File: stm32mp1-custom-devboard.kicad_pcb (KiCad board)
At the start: 4 copper layers, 120 x 80.6 mm, 137 parts, among them Con1 52746-0671, Con2 505110-2491, Con3 2041119-1, Con4 USB_C_Wurth_632723130112, Con5 USB_C_Wurth_632723130112, P1 Main Power Supply, Q1 BC847B, T2 WE-RJ45_74990101210, U1 TPS61169DCKR, U2 MCP1703T-3302E, U3 ST1S10PHR, U4 ST1S09IPUR, U5 STM32F103C(8-B)Tx, U6 MCP1700T-3302E_MB, U7 KSZ8041NL_RNL, U8 USBLC6-2, U9 USBLC6-2, X1 8.000MHZ, X2 ECS-2016MV-250-CN-TR

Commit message: Schematic finished, elements figurated on pcb, tracking started
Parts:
- added C54: 100n, Capacitors_Smd_0603:100nF_0603, F.Cu at (135.6, 135.4)
- added C55: 100n, Capacitors_Smd_0603:100nF_0603, F.Cu at (118.2, 133.8)
- added C56: 100n, Capacitors_Smd_0603:100nF_0603, F.Cu at (116.6, 133.2)
- added R51: 10k, Resistor_Smd_0603:10k_0603, F.Cu at (131.3, 128.7)
- added R52: 10k, Resistor_Smd_0603:10k_0603, F.Cu at (131.3, 126.2)
- added R53: 10k, Resistor_Smd_0603:10k_0603, F.Cu at (131.3, 133.7)
- added R54: 10k, Resistor_Smd_0603:10k_0603, F.Cu at (131.3, 131.2)
- added R55: 10k, Resistor_Smd_0603:10k_0603, F.Cu at (115.0, 131.0)
- added R56: 10k, Resistor_Smd_0603:10k_0603, F.Cu at (117.8, 130.2)
- added U10: APX803D-29SRG-7, Reset_Device_Diodes:APX803D-29SRG-7, F.Cu at (133.1, 136.0)
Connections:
- Con1 pad 6: /STM32MP1 module/PF10_GPIO -> /STM32MP1 module/PA9-GPIO
- Con2 pad 12: /LCD+Touchscreen/LCD_RESET -> /RESET
- Con3 pad 1: (no net) -> /STM32MP1 module/PE3-GPIO
- Con3 pad 10: (no net) -> /STM32MP1 module/SPI1_NSS
- Con3 pad 11: (no net) -> /STM32MP1 module/UART8-TXD
- Con3 pad 12: (no net) -> /STM32MP1 module/SPI1_MOSI
- Con3 pad 13: (no net) -> /STM32MP1 module/UART8-RXD
- Con3 pad 14: (no net) -> /STM32MP1 module/SPI1_MISO
- Con3 pad 15: (no net) -> GND
- Con3 pad 16: (no net) -> /STM32MP1 module/SPI1_SCK
- Con3 pad 18: (no net) -> GND
- Con3 pad 2: (no net) -> 3V3
- Con3 pad 20: (no net) -> /STM32MP1 module/PC7-GPIO
- Con3 pad 21: (no net) -> GND
- Con3 pad 22: (no net) -> /RESET
- Con3 pad 23: (no net) -> /STM32MP1 module/UART8-RTS
- Con3 pad 24: (no net) -> 3V3
- Con3 pad 25: (no net) -> /STM32MP1 module/UART8-CTS
- Con3 pad 26: (no net) -> GND
- Con3 pad 27: (no net) -> GND
- Con3 pad 29: (no net) -> GND
- Con3 pad 30: (no net) -> /MiniPci Module/I2C-SCL
- Con3 pad 32: (no net) -> /MiniPci Module/I2C-SDA
- Con3 pad 34: (no net) -> GND
- Con3 pad 35: (no net) -> GND
- Con3 pad 36: (no net) -> /USB Module/USB-A-D_M
- Con3 pad 37: (no net) -> GND
- Con3 pad 38: (no net) -> /USB Module/USB-A-D_P
- Con3 pad 39: (no net) -> 3V3
- Con3 pad 4: (no net) -> GND
- Con3 pad 40: (no net) -> GND
- Con3 pad 41: (no net) -> 3V3
- Con3 pad 42: (no net) -> /MiniPci Module/NETLIGHT
- Con3 pad 43: (no net) -> GND
- Con3 pad 45: (no net) -> /STM32MP1 module/PE14-GPIO
- Con3 pad 50: (no net) -> GND
- Con3 pad 52: (no net) -> 3V3
- Con3 pad 8: (no net) -> /PE15
- Con3 pad 9: (no net) -> GND
- Con5 pad A5: /USB Module/USB-C-ID -> /STM32MP1 module/PA0-GPIO
- Con5 pad B5: /USB Module/USB-C-ID -> /STM32MP1 module/PA0-GPIO
- R23 pad 1: /STLink Module/JTMS -> /STM32MP1 module/JTAG-TMS
- R34 pad 2: /Ethernet Module/ENET_MDC -> /STM32MP1 module/ENET1-MDC
- R50 pad 2: /USB Module/USB-C-ID -> /STM32MP1 module/PA0-GPIO
- SOM1 pad 10: (no net) -> Net-(R55-Pad2)
- SOM1 pad 100: Net-(SOM1-Pad100) -> 5V
- SOM1 pad 101: (no net) -> /Ethernet Module/ENET-CRS-DV
- SOM1 pad 102: Net-(SOM1-Pad100) -> 5V
- SOM1 pad 104: Net-(SOM1-Pad100) -> 5V
- SOM1 pad 106: Net-(SOM1-Pad100) -> 5V
- SOM1 pad 108: Net-(SOM1-Pad100) -> 5V
- SOM1 pad 109: (no net) -> /Arduino Shield Module/GPIO-D5
- SOM1 pad 110: Net-(SOM1-Pad100) -> 5V
- SOM1 pad 112: Net-(SOM1-Pad100) -> 5V
- SOM1 pad 113: (no net) -> /Arduino Shield Module/ATN
- SOM1 pad 114: (no net) -> /Ethernet Module/ENET-TXEN
- SOM1 pad 118: (no net) -> /STM32MP1 module/SPI1_MOSI
- SOM1 pad 119: (no net) -> /Ethernet Module/ENET-TXD2
- SOM1 pad 122: (no net) -> /Arduino Shield Module/GPIO-D6
- SOM1 pad 124: (no net) -> /Ethernet Module/ENET-TXD1
- SOM1 pad 129: (no net) -> /STM32MP1 module/PA9-GPIO
- SOM1 pad 131: (no net) -> /Arduino Shield Module/GPIO-D13
- SOM1 pad 134: (no net) -> /PE15
- SOM1 pad 137: (no net) -> /Arduino Shield Module/SPI-SCK
- SOM1 pad 138: (no net) -> /Ethernet Module/ENET-RXD2
- SOM1 pad 139: (no net) -> /STM32MP1 module/ADC1_INP2
- SOM1 pad 140: (no net) -> /STM32MP1 module/ADC1_INP19
- SOM1 pad 141: (no net) -> /STM32MP1 module/PC7-GPIO
- SOM1 pad 148: (no net) -> /Arduino Shield Module/GPIO-D11
- SOM1 pad 149: (no net) -> /STM32MP1 module/ADC1_INP15
- SOM1 pad 150: (no net) -> /Ethernet Module/ENET-RXER
- SOM1 pad 151: (no net) -> /Ethernet Module/ENET-TXD3
- SOM1 pad 152: (no net) -> /STM32MP1 module/ADC1_INP3
- SOM1 pad 154: (no net) -> /Arduino Shield Module/SPI-MISO
- SOM1 pad 157: /LCD+Touchscreen/LCD_RESET -> /Ethernet Module/ENET-REFCLK
- SOM1 pad 158: (no net) -> /Ethernet Module/ENET-IRQ
- SOM1 pad 160: (no net) -> /Arduino Shield Module/GPIO-D12
- SOM1 pad 161: (no net) -> /STM32MP1 module/PE14-GPIO
- SOM1 pad 162: (no net) -> /STM32MP1 module/SPI1_NSS
- SOM1 pad 163: (no net) -> /MiniPci Module/NETLIGHT
- SOM1 pad 164: (no net) -> /Arduino Shield Module/SPI-MOSI
- SOM1 pad 166: (no net) -> /Arduino Shield Module/I2C-SDA
- SOM1 pad 167: (no net) -> /Arduino Shield Module/UART-RX0
- SOM1 pad 169: (no net) -> /STM32MP1 module/SPI1_MISO
- SOM1 pad 171: (no net) -> /Arduino Shield Module/UART-TX0
- SOM1 pad 173: (no net) -> /Arduino Shield Module/GPIO-D3
- SOM1 pad 175: (no net) -> /STM32MP1 module/SPI1_SCK
- SOM1 pad 179: (no net) -> /STM32MP1 module/PE3-GPIO
- SOM1 pad 19: (no net) -> /USB Module/USB-C-D_P
- SOM1 pad 21: (no net) -> /USB Module/USB-C-D_M
- SOM1 pad 25: (no net) -> /USB Module/USB-A-D_P
- SOM1 pad 27: (no net) -> /USB Module/USB-A-D_M
- SOM1 pad 4: (no net) -> /RESET
- SOM1 pad 45: (no net) -> /Arduino Shield Module/GPIO-D4
- SOM1 pad 46: (no net) -> /STM32MP1 module/JTAG-TMS
- SOM1 pad 47: (no net) -> /STM32MP1 module/ADC1_INP13
- SOM1 pad 48: (no net) -> /STM32MP1 module/JTAG-~TRST~
- SOM1 pad 52: (no net) -> /STM32MP1 module/JTAG-TDO
- SOM1 pad 53: (no net) -> /STM32MP1 module/ENET1-MDC
- SOM1 pad 54: (no net) -> /STM32MP1 module/JTAG-TCK
- SOM1 pad 55: (no net) -> /STM32MP1 module/ADC2_INP10
- SOM1 pad 57: (no net) -> /STM32MP1 module/UART8-TXD
- SOM1 pad 58: (no net) -> /Ethernet Module/ENET-RXD3
- SOM1 pad 6: (no net) -> Net-(C55-Pad1)
- SOM1 pad 61: (no net) -> /Ethernet Module/ENET-MDIO
- SOM1 pad 62: (no net) -> /STM32MP1 module/PA0-GPIO
- SOM1 pad 63: (no net) -> /STM32MP1 module/UART8-RXD
- SOM1 pad 64: /STM32MP1 module/PF10_GPIO -> /Arduino Shield Module/GPIO-D2
- SOM1 pad 65: (no net) -> /Arduino Shield Module/GPIO-D8
- SOM1 pad 66: (no net) -> /STM32MP1 module/UART8-CTS
- SOM1 pad 67: (no net) -> /Arduino Shield Module/GPIO-D7
- SOM1 pad 69: (no net) -> /Arduino Shield Module/SPI-RST
- SOM1 pad 7: (no net) -> Net-(R53-Pad2)
- SOM1 pad 72: (no net) -> /Arduino Shield Module/GPIO-D10
- SOM1 pad 73: (no net) -> /Arduino Shield Module/I2C-SCL
- SOM1 pad 74: (no net) -> /STM32MP1 module/UART8-RTS
- SOM1 pad 75: (no net) -> /STLink Module/STLINK_RX
- SOM1 pad 76: (no net) -> /MiniPci Module/I2C-SCL
- SOM1 pad 77: (no net) -> /STLink Module/STLINK_TX
- SOM1 pad 78: (no net) -> /Arduino Shield Module/GPIO-D9
- SOM1 pad 79: (no net) -> /Ethernet Module/ENET-TXD0
- SOM1 pad 8: (no net) -> Net-(C56-Pad1)
- SOM1 pad 80: (no net) -> /MiniPci Module/I2C-SDA
- SOM1 pad 9: (no net) -> Net-(R51-Pad2)
- SOM1 pad 96: Net-(SOM1-Pad100) -> 5V
- SOM1 pad 97: (no net) -> /Ethernet Module/ENET-RXD0
- SOM1 pad 98: Net-(SOM1-Pad100) -> 5V
- SOM1 pad 99: (no net) -> /Ethernet Module/ENET-RXD1
- U5 pad 12: (no net) -> /STLink Module/STLINK_TX
- U5 pad 13: (no net) -> /STLink Module/STLINK_RX
- U5 pad 18: (no net) -> /STM32MP1 module/JTAG-~TRST~
- U5 pad 26: (no net) -> /STM32MP1 module/JTAG-TCK
- U5 pad 27: /STLink Module/JTMS -> /STM32MP1 module/JTAG-TMS
- U5 pad 31: (no net) -> /STM32MP1 module/JTAG-TDO
- U7 pad 12: /Ethernet Module/ENET_MDC -> /STM32MP1 module/ENET1-MDC
- U7 pad 23: (no net) -> /Ethernet Module/ENET-TXEN
- U7 pad 24: (no net) -> /Ethernet Module/ENET-TXD0
- U7 pad 25: (no net) -> /Ethernet Module/ENET-TXD1
- U7 pad 26: (no net) -> /Ethernet Module/ENET-TXD2
- U7 pad 27: (no net) -> /Ethernet Module/ENET-TXD3
- U8 pad 1: (no net) -> /USB Module/USB-C-D_M
- U8 pad 3: (no net) -> /USB Module/USB-C-D_P
- U9 pad 1: (no net) -> /USB Module/USB-A-D_M
- U9 pad 3: (no net) -> /USB Module/USB-A-D_P
- XA1 pad A0: (no net) -> /STM32MP1 module/ADC1_INP2
- XA1 pad A1: (no net) -> /STM32MP1 module/ADC2_INP10
- XA1 pad A2: (no net) -> /STM32MP1 module/ADC1_INP13
- XA1 pad A3: (no net) -> /STM32MP1 module/ADC1_INP15
- XA1 pad A4: (no net) -> /STM32MP1 module/ADC1_INP3
- XA1 pad A5: (no net) -> /STM32MP1 module/ADC1_INP19
- XA1 pad ATN: (no net) -> /Arduino Shield Module/ATN
- XA1 pad D0: (no net) -> /Arduino Shield Module/UART-RX0
- XA1 pad D1: (no net) -> /Arduino Shield Module/UART-TX0
- XA1 pad D10: (no net) -> /Arduino Shield Module/GPIO-D10
- XA1 pad D11: (no net) -> /Arduino Shield Module/GPIO-D11
- XA1 pad D12: (no net) -> /Arduino Shield Module/GPIO-D12
- XA1 pad D13: (no net) -> /Arduino Shield Module/GPIO-D13
- XA1 pad D2: (no net) -> /Arduino Shield Module/GPIO-D2
- XA1 pad D3: (no net) -> /Arduino Shield Module/GPIO-D3
- XA1 pad D4: (no net) -> /Arduino Shield Module/GPIO-D4
- XA1 pad D5: (no net) -> /Arduino Shield Module/GPIO-D5
- XA1 pad D6: (no net) -> /Arduino Shield Module/GPIO-D6
- XA1 pad D7: (no net) -> /Arduino Shield Module/GPIO-D7
- XA1 pad D8: (no net) -> /Arduino Shield Module/GPIO-D8
- XA1 pad D9: (no net) -> /Arduino Shield Module/GPIO-D9
- XA1 pad IORF: (no net) -> /PE15
- XA1 pad MISO: (no net) -> /Arduino Shield Module/SPI-MISO
- XA1 pad MOSI: (no net) -> /Arduino Shield Module/SPI-MOSI
- XA1 pad RST1: (no net) -> /RESET
- XA1 pad RST2: (no net) -> /Arduino Shield Module/SPI-RST
- XA1 pad SCK: (no net) -> /Arduino Shield Module/SPI-SCK
- XA1 pad SCL: (no net) -> /Arduino Shield Module/I2C-SCL
- XA1 pad SDA: (no net) -> /Arduino Shield Module/I2C-SDA

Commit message: Tracking in progress
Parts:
- moved C54 2.88 mm to (136.2, 132.6), turned to 180 degrees
- moved R8 1.52 mm to (185.5, 108.5)
- moved R7 1.33 mm to (186.9, 108.5)
- moved C9 0.26 mm to (139.2, 98.9)
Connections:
- Con5 pad B3: (no net) -> /STM32MP1 module/PA0-GPIO
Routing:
- net GND: track 0.00 -> 157.2 mm, vias 0 -> 77
- net 3V3: track 0.00 -> 131.5 mm, vias 0 -> 10
- net /LCD+Touchscreen/Touchscreen Power Supply/VOUT_3.3V_250mA: track 0.00 -> 47.7 mm
- net 5V: track 0.00 -> 44.7 mm, vias 0 -> 11
- net VPP: track 0.00 -> 35.5 mm, vias 0 -> 3
- net /LCD+Touchscreen/LCD Backlight Controller/BACKLIGHT_HIGH: track 0.00 -> 28.9 mm, vias 0 -> 2
- net /LCD+Touchscreen/LCD Backlight Controller/BACKLIGHT_LOW: track 0.00 -> 28.7 mm, vias 0 -> 2
- net Net-(C10-Pad1): track 0.00 -> 28.0 mm, vias 0 -> 2
- net Net-(C49-Pad2): track 0.00 -> 25.7 mm
- net Net-(C26-Pad2): track 0.00 -> 25.7 mm
- net Net-(C6-Pad1): track 0.00 -> 18.7 mm
- net /STM32MP1 module/PA0-GPIO: track 0.00 -> 18.2 mm, vias 0 -> 3
- net Net-(C45-Pad2): track 0.00 -> 17.0 mm
- net /RESET: track 0.00 -> 15.0 mm
- net Net-(C15-Pad2): track 0.00 -> 14.9 mm, vias 0 -> 2
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- added copper zone on In1.Cu, net 5V
- removed copper zone on In1.Cu, net 3V3
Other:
- net class USB-C added: clearance 0.152, trace_width 0.152, via_dia 0.45, via_drill 0.2
- rule trace_min: 0.2 -> 0.152

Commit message: Tracking in progress
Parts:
- moved R94 2.54 mm to (194.3, 130.4), turned to 0 degrees
- moved R49 2.52 mm to (193.5, 127.8), turned to 90 degrees
- moved R48 1.56 mm to (194.3, 129.4), turned to 0 degrees
- moved R96 1.44 mm to (194.5, 127.8), turned to 90 degrees
- moved R27 0.39 mm to (185.6, 132.2)
- moved C35 0.37 mm to (193.9, 131.6)
- moved R41 0.24 mm to (191.8, 126.2)
- moved C12 0.12 mm to (146.5, 108.6)
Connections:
- net /USB Module/USB-A-D_M renamed /USB Module/USB-A-D_N
- net /USB Module/USB-C-D_M renamed /USB Module/USB-C-D_N
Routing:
- net 3V3: track 131.5 -> 442.6 mm, vias 10 -> 28
- net /Arduino Shield Module/UART-RX0: track 0.00 -> 132.7 mm, vias 0 -> 3
- net /Arduino Shield Module/UART-TX0: track 0.00 -> 129.7 mm, vias 0 -> 3
- net /Arduino Shield Module/GPIO-D3: track 0.00 -> 127.5 mm, vias 0 -> 3
- net /Arduino Shield Module/SPI-MISO: track 0.00 -> 102.9 mm, vias 0 -> 1
- net /Arduino Shield Module/SPI-MOSI: track 0.00 -> 102.9 mm, vias 0 -> 1
- net /LCD+Touchscreen/LCD_MIPI_D0-: track 0.00 -> 97.2 mm, vias 0 -> 2
- net /LCD+Touchscreen/LCD_MIPI_D0+: track 0.00 -> 93.3 mm, vias 0 -> 2
- net /LCD+Touchscreen/LCD_MIPI_D1-: track 0.00 -> 89.9 mm, vias 0 -> 2
- net /Arduino Shield Module/GPIO-D6: track 0.00 -> 89.3 mm, vias 0 -> 3
- net /USB Module/USB-C-D_P: track 0.00 -> 87.7 mm, vias 0 -> 2
- net /Arduino Shield Module/SPI-SCK: track 0.00 -> 87.6 mm, vias 0 -> 4
- net /LCD+Touchscreen/LCD_MIPI_D1+: track 0.00 -> 86.7 mm, vias 0 -> 2
- net /USB Module/USB-C-D_N: track 0.00 -> 85.6 mm, vias 0 -> 2
- net /Arduino Shield Module/GPIO-D2: track 0.00 -> 80.2 mm, vias 0 -> 1
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
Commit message: Tracking almost finished
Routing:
- net /Ethernet Module/ENET-TXD1: track 0.98 -> 130.9 mm, vias 1 -> 4
- net /Ethernet Module/ENET-TXD3: track 3.03 -> 132.4 mm, vias 1 -> 8
- net /STM32MP1 module/JTAG-TMS: track 2.84 -> 131.2 mm, vias 0 -> 4
- net /Ethernet Module/ENET-IRQ: track 2.15 -> 126.5 mm, vias 0 -> 4
- net /STM32MP1 module/JTAG-TDO: track 0.00 -> 124.2 mm, vias 0 -> 4
- net /Ethernet Module/ENET-TXD0: track 0.66 -> 119.1 mm, vias 1 -> 4
- net /LCD+Touchscreen/LCD_BACKLIGHT_PWM: track 0.00 -> 116.0 mm, vias 0 -> 4
- net /STM32MP1 module/JTAG-TCK: track 0.00 -> 111.7 mm, vias 0 -> 4
- net /Ethernet Module/ENET-RXER: track 8.61 -> 119.4 mm, vias 0 -> 4
- net /STM32MP1 module/JTAG-~TRST~: track 0.00 -> 109.2 mm, vias 0 -> 4
- net /Ethernet Module/ENET-TXEN: track 0.75 -> 108.6 mm, vias 1 -> 4
- net /STM32MP1 module/PA0-GPIO: track 18.2 -> 122.2 mm, vias 3 -> 6
- net /STM32MP1 module/PE2_I2C4_SDA: track 12.0 -> 114.9 mm, vias 0 -> 8
- net /Ethernet Module/ENET-RXD2: track 6.93 -> 108.5 mm, vias 2 -> 7
- net /STM32MP1 module/PA9-GPIO: track 0.69 -> 100.0 mm, vias 1 -> 6
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
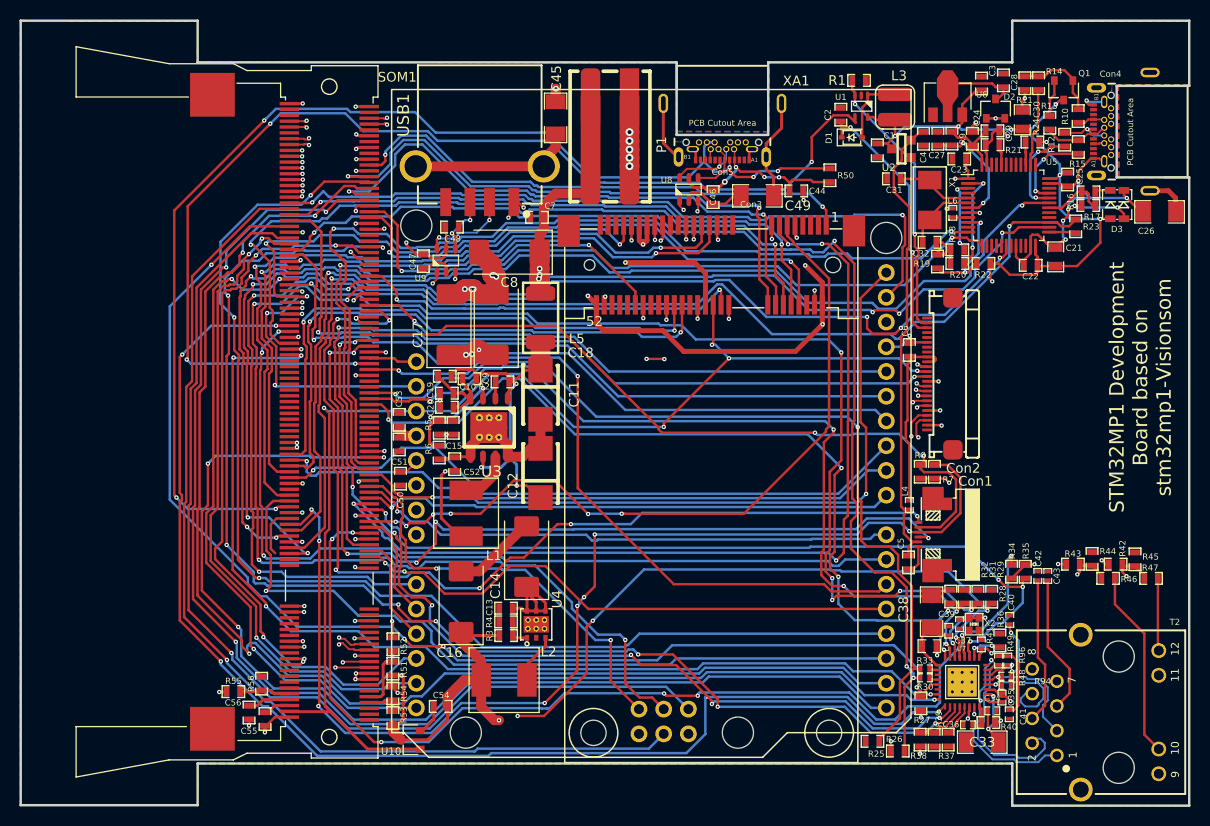
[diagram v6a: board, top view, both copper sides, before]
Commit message: Tracking finished, started tunning
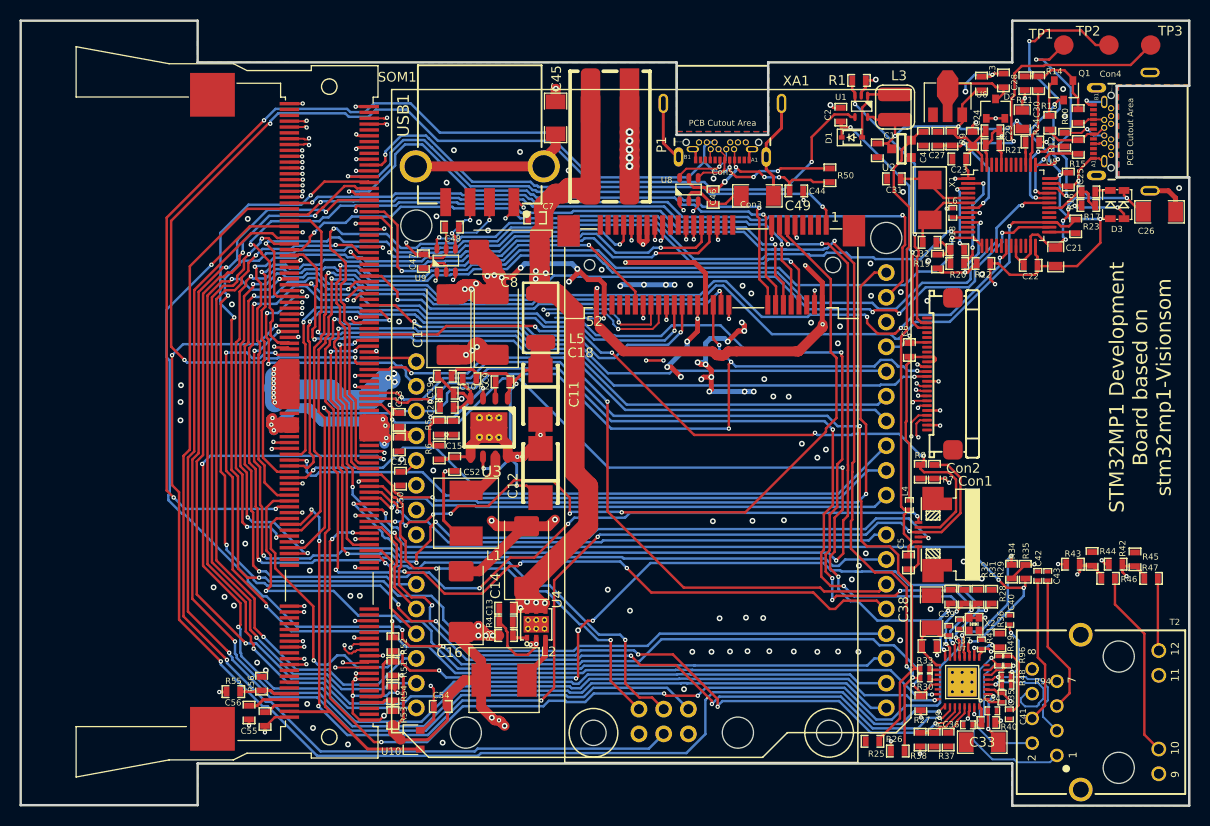
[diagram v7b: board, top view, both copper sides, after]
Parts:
- added TP1: SWDIO_PRG, Test_Points:Test_Point_2.54mm, F.Cu at (200.2, 64.6)
- added TP2: SWCLK_PRG, Test_Points:Test_Point_2.54mm, F.Cu at (204.9, 64.6)
- added TP3: ~RESET~_PRG, Test_Points:Test_Point_2.54mm, F.Cu at (209.2, 64.6)
- moved C7 0.21 mm to (145.9, 82.4)
- moved C25 0.07 mm to (200.7, 78.4)
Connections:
- net Net-(C27-Pad1) renamed /STLink Module/STM-JTMS-~RESET~
- U5 pad 34: (no net) -> /STLink Module/STM-JTMS-SWDIO
- U5 pad 37: (no net) -> /STLink Module/STM-JTCK-SWCLK
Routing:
- net 3V3: track 455.7 -> 568.0 mm, vias 28 -> 34
- net 5V: track 57.7 -> 161.1 mm, vias 14 -> 42
- net VPP: track 35.5 -> 118.1 mm, vias 3 -> 7
- net GND: track 239.2 -> 314.4 mm, vias 100 -> 202
- net Net-(SOM1-Pad85): track 0.00 -> 51.2 mm, vias 0 -> 7
- net /Ethernet Module/ENET-RXD3: track 72.1 -> 107.4 mm, vias 4 -> 8
- net /STLink Module/STM-JTMS-~RESET~: track 12.0 -> 39.7 mm, vias 2 -> 3
- net /USB Module/USB-A-D_P: track 50.3 -> 77.6 mm, vias 2 -> 4
- net /USB Module/USB-A-D_N: track 50.0 -> 77.0 mm, vias 2 -> 4
- net /STLink Module/STM-JTCK-SWCLK: track 0.00 -> 25.7 mm, vias 0 -> 2
- net /STLink Module/STM-JTMS-SWDIO: track 0.00 -> 22.3 mm, vias 0 -> 2
- net /USB Module/USB-C-D_N: track 85.7 -> 91.3 mm
- net /USB Module/USB-C-D_P: track 87.6 -> 92.9 mm
- net /Ethernet Module/ETH_TX_N: track 23.4 -> 18.5 mm
- net /RESET: track 122.9 -> 127.8 mm
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
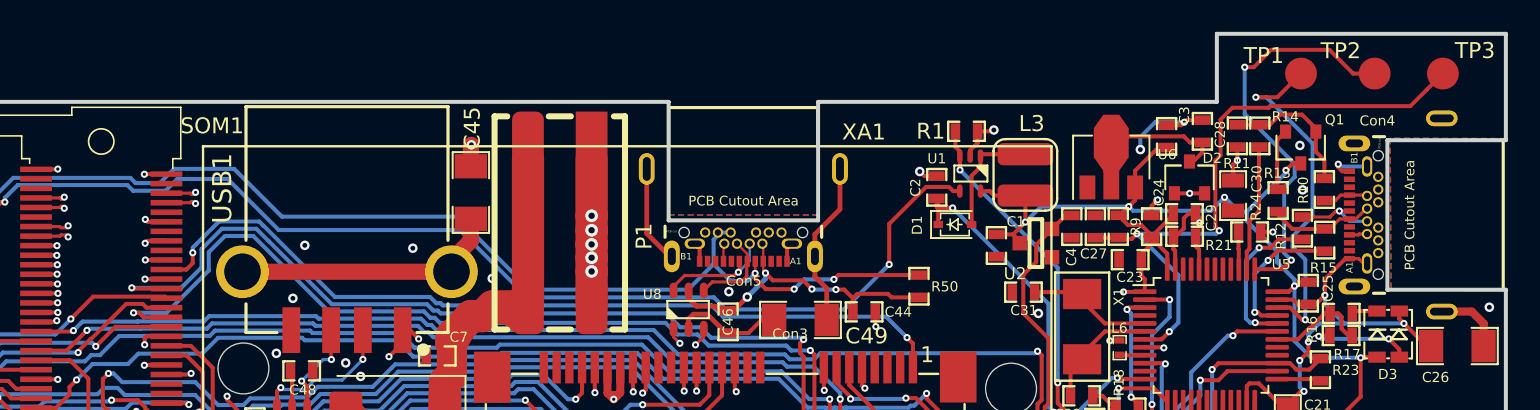
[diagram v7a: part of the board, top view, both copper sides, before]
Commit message: Added gnd in stm32f swd interface
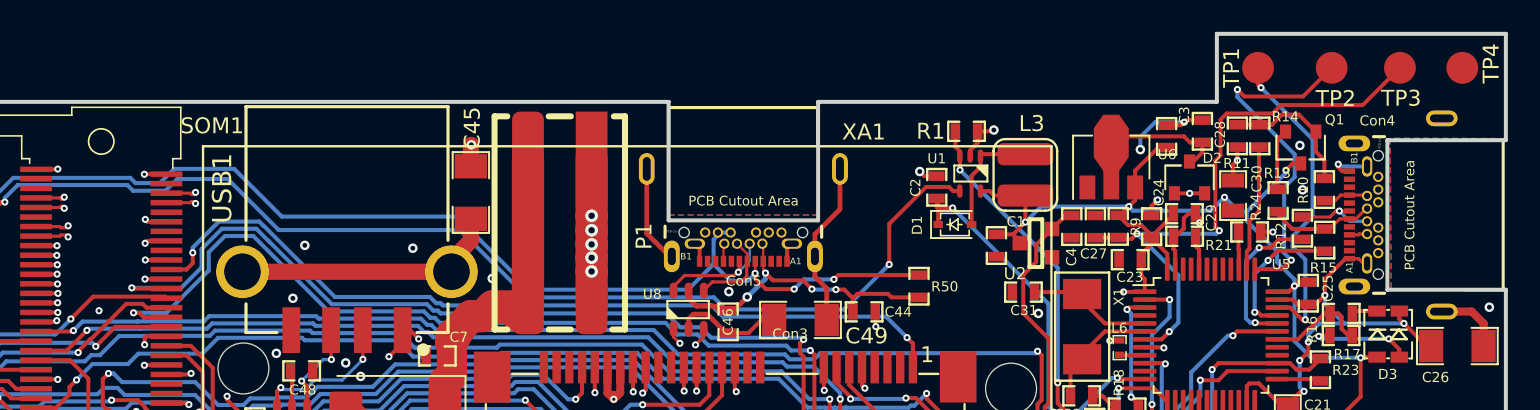
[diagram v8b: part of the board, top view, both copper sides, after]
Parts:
- added TP4: GND, Test_Points:Test_Point_2.54mm, F.Cu at (210.4, 64.3)
- moved TP2 2.72 mm to (202.2, 64.3)
- moved TP3 2.72 mm to (206.4, 64.3)
- moved TP1 2.72 mm to (197.5, 64.3)
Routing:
- net /STLink Module/STM-JTCK-SWCLK: track 25.7 -> 22.1 mm
- net /STLink Module/STM-JTMS-~RESET~: track 39.7 -> 37.1 mm
- net /STLink Module/STM-JTMS-SWDIO: track 22.3 -> 20.2 mm
- net GND: vias 202 -> 203
